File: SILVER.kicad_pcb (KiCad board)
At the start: 2 copper layers, 2 parts, among them J1 Conn_02x22, J2 Conn_02x22

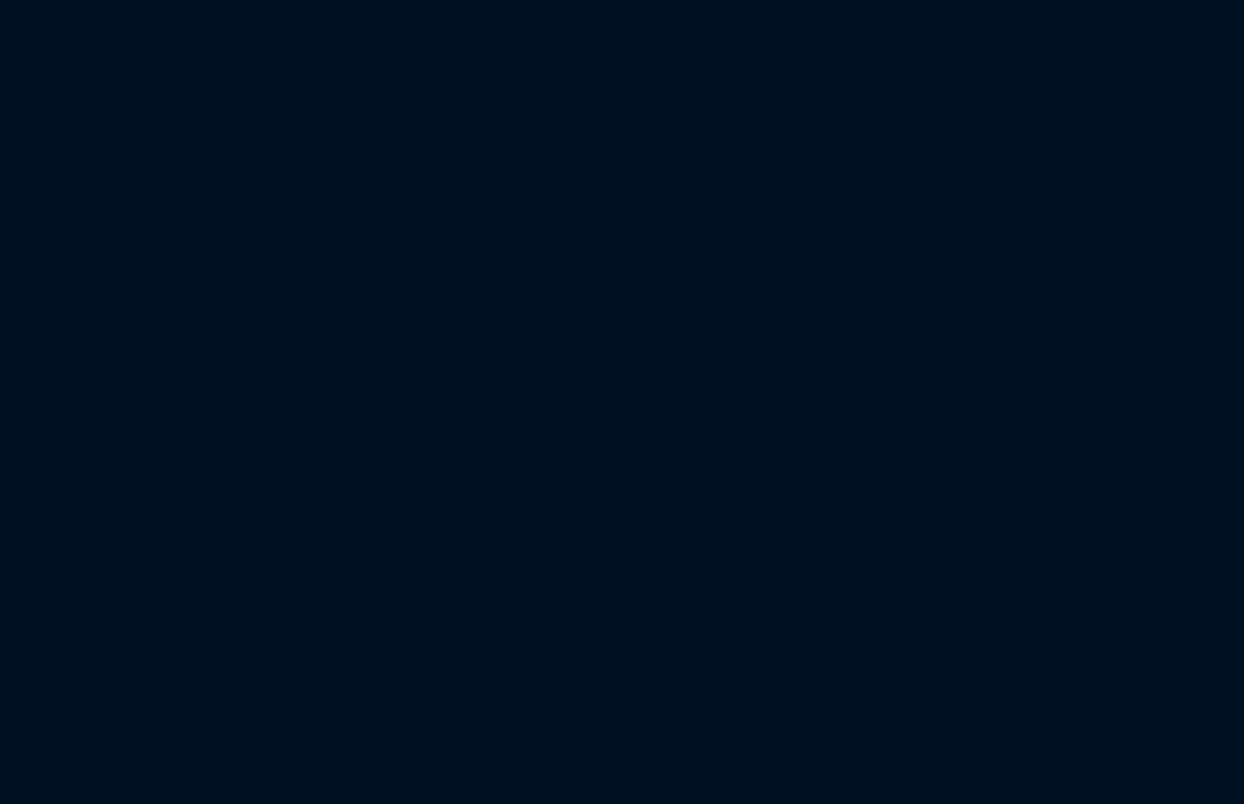
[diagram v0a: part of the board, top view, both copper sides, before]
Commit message: feat: Add new dc-dc converter and VNH5019 motor driver projects, update main schematic with motor connectors.
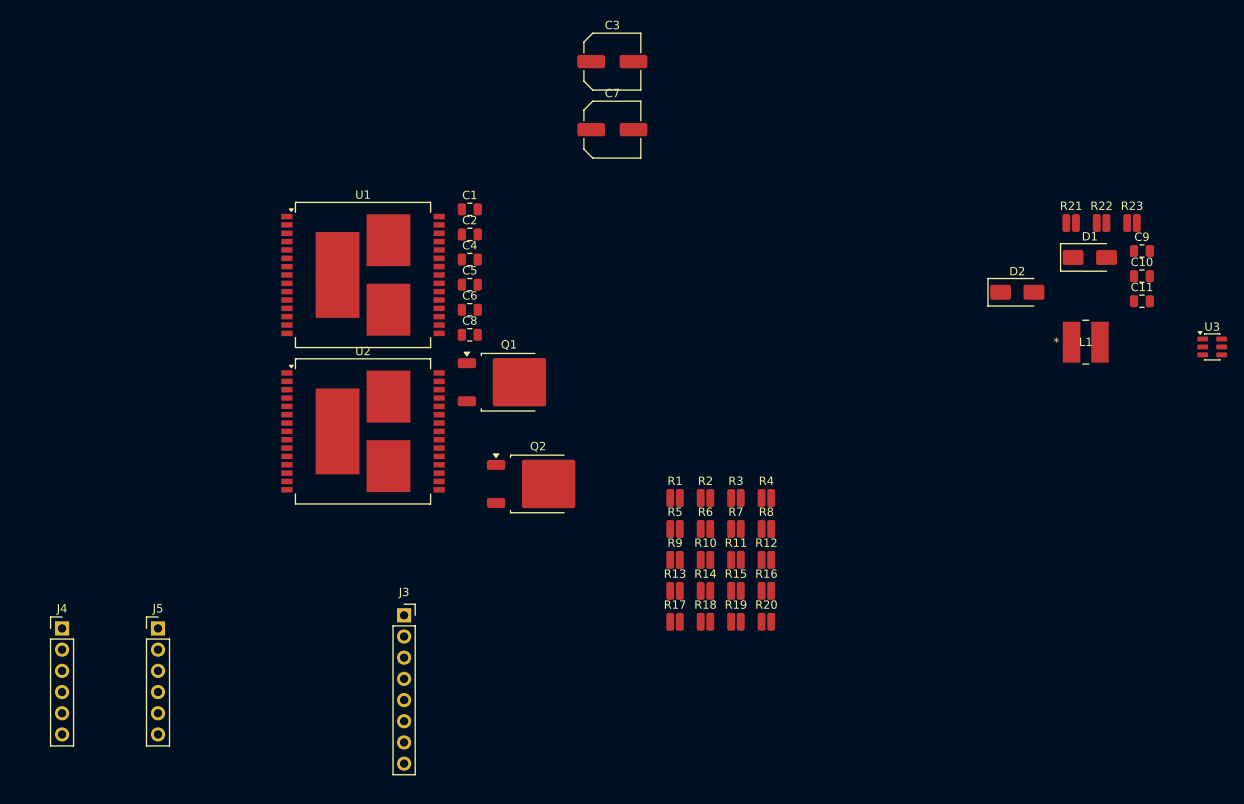
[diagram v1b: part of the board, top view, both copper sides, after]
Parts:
- added C1: 33nF, Capacitor_SMD:C_0805_2012Metric, F.Cu at (137.4, 40.6)
- added C10: 10nF, Capacitor_SMD:C_0805_2012Metric, F.Cu at (217.9, 48.6)
- added C11: 22uF 10v, Capacitor_SMD:C_0805_2012Metric, F.Cu at (217.9, 51.6)
- added C2: 0.1u, Capacitor_SMD:C_0805_2012Metric, F.Cu at (137.4, 43.6)
- added C3: 47uF, Capacitor_SMD:C_Elec_6.3x5.4, F.Cu at (154.5, 22.9)
- added C4: 0.1u, Capacitor_SMD:C_0805_2012Metric, F.Cu at (137.4, 46.6)
- added C5: 33nF, Capacitor_SMD:C_0805_2012Metric, F.Cu at (137.4, 49.6)
- added C6: 0.1u, Capacitor_SMD:C_0805_2012Metric, F.Cu at (137.4, 52.6)
- added C7: 47uF, Capacitor_SMD:C_Elec_6.3x5.4, F.Cu at (154.5, 31.0)
- added C8: 0.1u, Capacitor_SMD:C_0805_2012Metric, F.Cu at (137.4, 55.6)
- added C9: 10uF 25v, Capacitor_SMD:C_0805_2012Metric, F.Cu at (217.9, 45.6)
- added D1: SS24, Diode_SMD:D_SMA, F.Cu at (211.7, 46.3)
- added D2: SS24, Diode_SMD:D_SMA, F.Cu at (203.0, 50.5)
- added J3: MPU6050, Connector_PinSocket_2.54mm:PinSocket_1x08_P2.54mm_Vertical, F.Cu at (129.5, 89.2)
- added J4: MotorL, Connector_PinHeader_2.54mm:PinHeader_1x06_P2.54mm_Vertical, F.Cu at (88.5, 90.8)
- added J5: motorR, Connector_PinHeader_2.54mm:PinHeader_1x06_P2.54mm_Vertical, F.Cu at (100.0, 90.8)
- added L1: 4.7uH, Library:IND_5028_TDK, F.Cu at (211.2, 56.5)
- added Q1: FCD600N60Z, Package_TO_SOT_SMD:TO-252-2, F.Cu at (142.1, 61.3)
- added Q2: FCD600N60Z, Package_TO_SOT_SMD:TO-252-2, F.Cu at (145.6, 73.5)
- added R1: 10k, Resistor_SMD:R_0508_1220Metric, F.Cu at (162.0, 75.2)
- added R10: 10k, Resistor_SMD:R_0508_1220Metric, F.Cu at (165.6, 82.6)
- added R11: 1k, Resistor_SMD:R_0508_1220Metric, F.Cu at (169.3, 82.6)
- added R12: 1k, Resistor_SMD:R_0508_1220Metric, F.Cu at (172.9, 82.6)
- added R13: 1k, Resistor_SMD:R_0508_1220Metric, F.Cu at (162.0, 86.3)
- added R14: 1k, Resistor_SMD:R_0508_1220Metric, F.Cu at (165.6, 86.3)
- added R15: 1k, Resistor_SMD:R_0508_1220Metric, F.Cu at (169.3, 86.3)
- added R16: 1k, Resistor_SMD:R_0508_1220Metric, F.Cu at (172.9, 86.3)
- added R17: 4.7k, Resistor_SMD:R_0508_1220Metric, F.Cu at (162.0, 90.0)
- added R18: 10k, Resistor_SMD:R_0508_1220Metric, F.Cu at (165.6, 90.0)
- added R19: 4.7k, Resistor_SMD:R_0508_1220Metric, F.Cu at (169.3, 90.0)
- added R2: 1k, Resistor_SMD:R_0508_1220Metric, F.Cu at (165.6, 75.2)
- added R20: 4.7k, Resistor_SMD:R_0508_1220Metric, F.Cu at (172.9, 90.0)
- added R21: 100K, Resistor_SMD:R_0508_1220Metric, F.Cu at (209.5, 42.2)
- added R22: 49.9K, Resistor_SMD:R_0508_1220Metric, F.Cu at (213.1, 42.2)
- added R23: 9.53K, Resistor_SMD:R_0508_1220Metric, F.Cu at (216.8, 42.2)
- added R3: 1k, Resistor_SMD:R_0508_1220Metric, F.Cu at (169.3, 75.2)
- added R4: 1k, Resistor_SMD:R_0508_1220Metric, F.Cu at (172.9, 75.2)
- added R5: 1k, Resistor_SMD:R_0508_1220Metric, F.Cu at (162.0, 78.9)
- added R6: 1k, Resistor_SMD:R_0508_1220Metric, F.Cu at (165.6, 78.9)
- added R7: 1k, Resistor_SMD:R_0508_1220Metric, F.Cu at (169.3, 78.9)
- added R8: 4.7k, Resistor_SMD:R_0508_1220Metric, F.Cu at (172.9, 78.9)
- added R9: 10k, Resistor_SMD:R_0508_1220Metric, F.Cu at (162.0, 82.6)
- added U1: VNH5019A-E, Package_SO:ST_MultiPowerSO-30, F.Cu at (124.6, 48.4)
- added U2: VNH5019A-E, Package_SO:ST_MultiPowerSO-30, F.Cu at (124.6, 67.2)
- added U3: MP2359DJ-LF-Z, Package_TO_SOT_SMD:SOT-23-6, F.Cu at (226.4, 57.0)

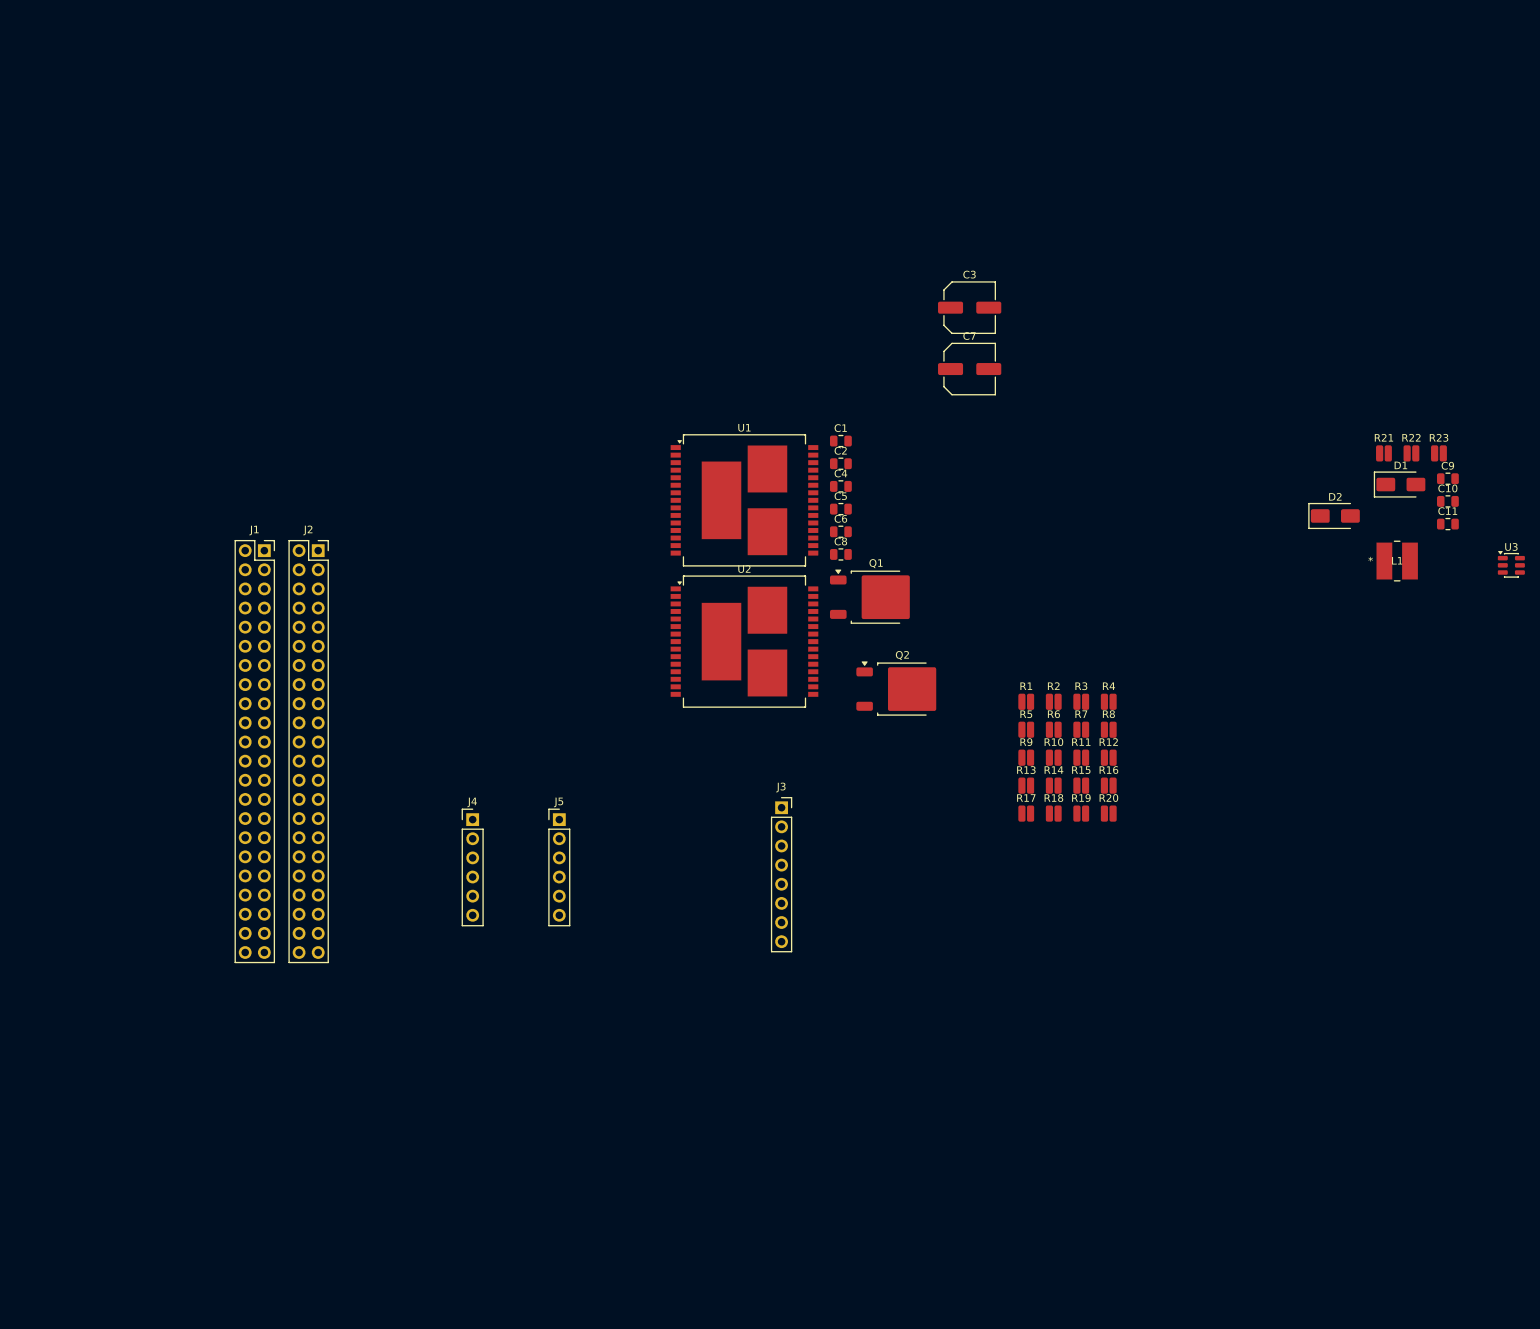
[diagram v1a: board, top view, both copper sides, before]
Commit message: feat: Introduce LM2596 and STLINK KiCad projects with new symbols and footprints, and update the main SILVER project.
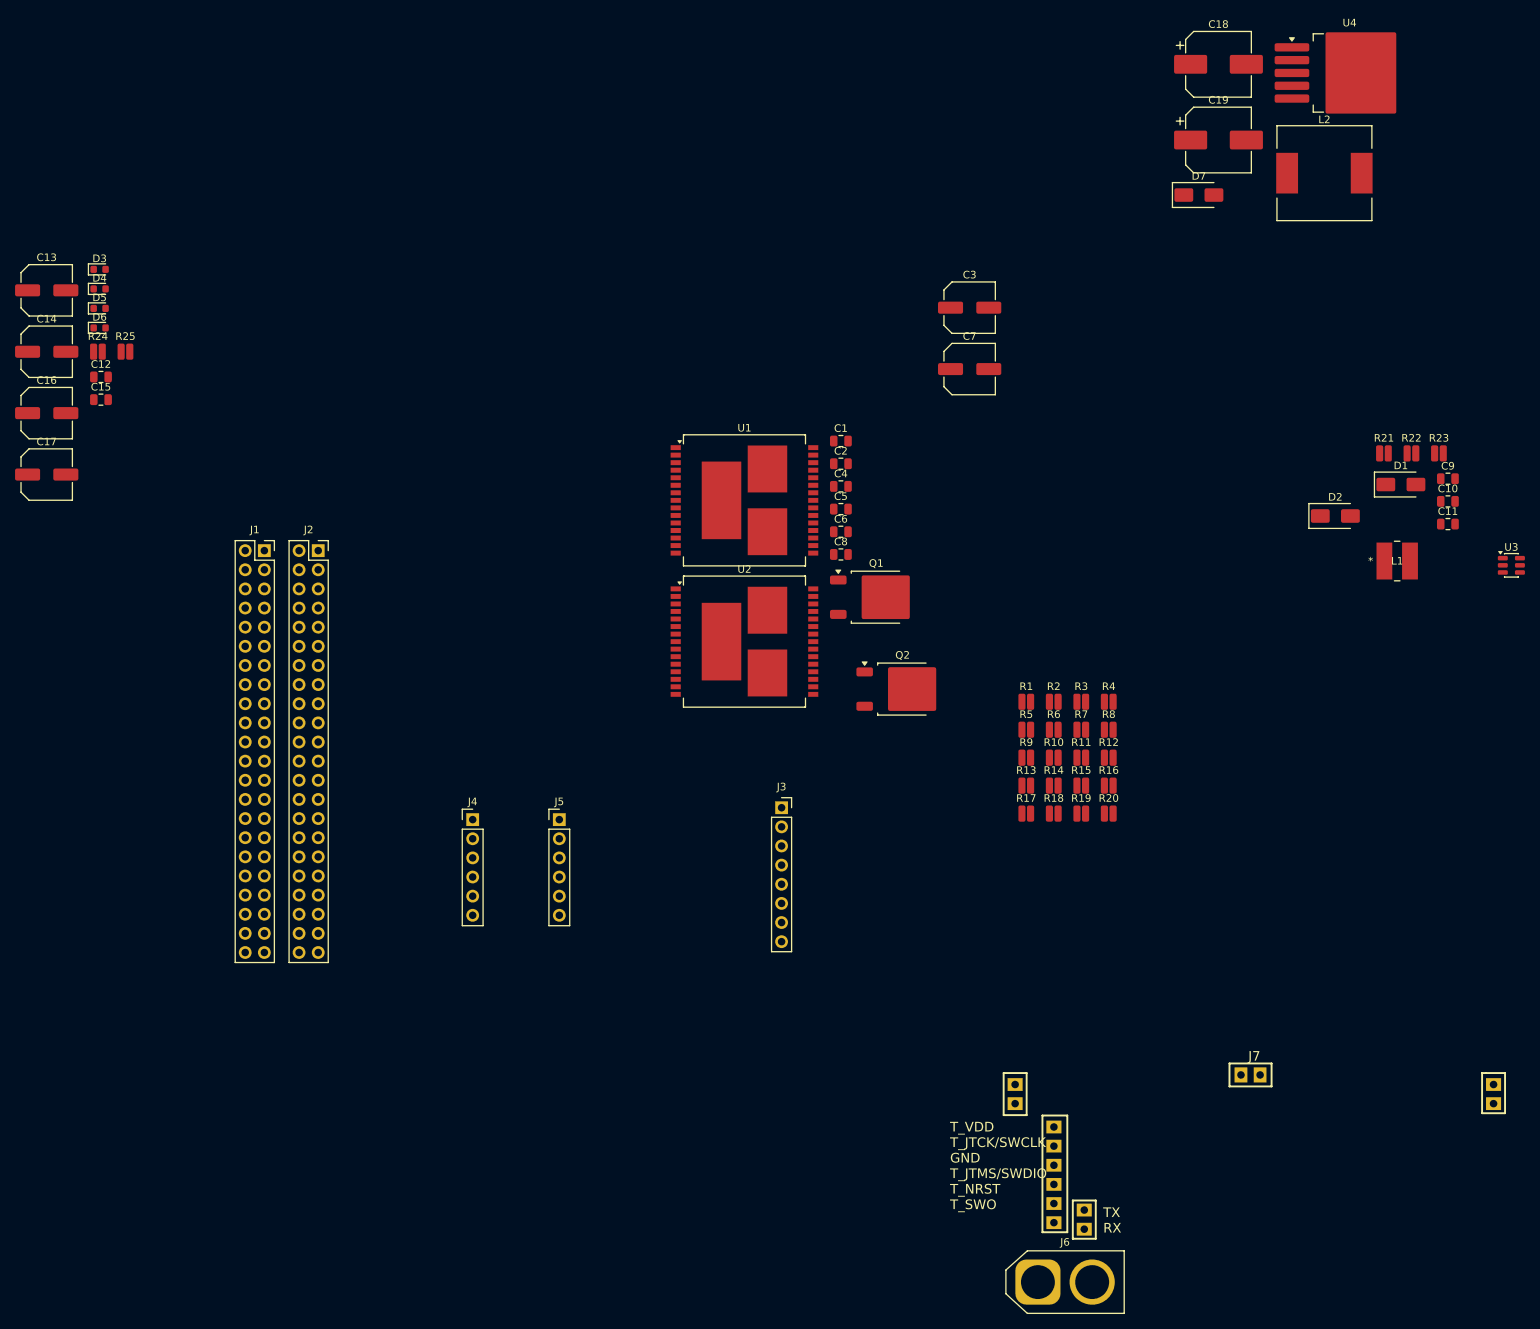
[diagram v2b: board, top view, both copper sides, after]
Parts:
- added C12: 0.1u, Capacitor_SMD:C_0805_2012Metric, F.Cu at (39.2, 32.0)
- added C13: NP, Capacitor_SMD:C_Elec_6.3x5.4, F.Cu at (32.0, 20.6)
- added C14: NP, Capacitor_SMD:C_Elec_6.3x5.4, F.Cu at (32.0, 28.7)
- added C15: 0.1u, Capacitor_SMD:C_0805_2012Metric, F.Cu at (39.2, 35.1)
- added C16: NP, Capacitor_SMD:C_Elec_6.3x5.4, F.Cu at (32.0, 36.9)
- added C17: NP, Capacitor_SMD:C_Elec_6.3x5.4, F.Cu at (32.0, 45.0)
- added C18: 330u, Capacitor_SMD:CP_Elec_8x10.5, F.Cu at (187.5, -9.45)
- added C19: 330u, Capacitor_SMD:CP_Elec_8x10.5, F.Cu at (187.5, 0.60)
- added D3: GREEN, LED_SMD:LED_0603_1608Metric, F.Cu at (39.0, 17.8)
- added D4: RED, LED_SMD:LED_0603_1608Metric, F.Cu at (39.0, 20.4)
- added D5: RED, LED_SMD:LED_0603_1608Metric, F.Cu at (39.0, 22.9)
- added D6: GREEN, LED_SMD:LED_0603_1608Metric, F.Cu at (39.0, 25.5)
- added D7: SS34, Diode_SMD:D_SMA, F.Cu at (184.9, 7.90)
- added J6: XT60-M, Connector_AMASS:AMASS_XT60-M_1x02_P7.20mm_Vertical, F.Cu at (163.5, 152.2)
- added J7: STLINK, Library:STLINK, F.Cu at (192.2, 134.9)
- added L2: 47uH, Inductor_SMD:L_12x12mm_H6mm, F.Cu at (201.6, 5.00)
- added R24: 4.7k, Resistor_SMD:R_0508_1220Metric, F.Cu at (38.8, 28.7)
- added R25: 4.7k, Resistor_SMD:R_0508_1220Metric, F.Cu at (42.4, 28.7)
- added U4: LM2596S-5.0, Package_TO_SOT_SMD:TO-263-5_TabPin3, F.Cu at (204.9, -8.30)
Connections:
- C2 pad 2: /12V -> +12V
- C3 pad 1: Net-(Q1-S) -> VOUT
- C4 pad 1: Net-(Q1-S) -> VOUT
- C7 pad 1: Net-(Q2-S) -> VOUT
- C8 pad 1: Net-(Q2-S) -> VOUT
- Q1 pad 3: Net-(Q1-S) -> VOUT
- Q2 pad 3: Net-(Q2-S) -> VOUT
- U1 pad 12: /12V -> +12V
- U1 pad 13: Net-(Q1-S) -> VOUT
- U1 pad 23: Net-(Q1-S) -> VOUT
- U1 pad 3: Net-(Q1-S) -> VOUT
- U1 pad 5: Net-(U1-ENADIAGA) -> +5V
- U1 pad 9: Net-(U1-ENBDIAGB) -> +5V
- U2 pad 13: Net-(Q2-S) -> VOUT
- U2 pad 23: Net-(Q2-S) -> VOUT
- U2 pad 3: Net-(Q2-S) -> VOUT
- U2 pad 5: Net-(U2-ENADIAGA) -> +5V
- U2 pad 9: Net-(U2-ENBDIAGB) -> +5V
